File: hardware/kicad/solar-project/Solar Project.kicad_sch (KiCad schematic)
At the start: 129 parts, among them J1 Solar In, J3 Battery Bus, J4 JTAG, J5 Connector,_USB-TYPE-C-16P, M1 IPZ40N, M2 Q_NMOS, M3 Q_NMOS, M4 Q_NMOS, Q1 BSS138, Q2 BSS138, U1 STM32G431CBU6, U2 BSC112N06LD, U3 CP2102-GMR, U4 LM5163DDAR, U5 BSC155N06ND, U6 LM51772QRHARQ1, U7 AHT20

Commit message: Clean DRC and update handoff
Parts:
- removed J5: Connector,_USB-TYPE-C-16P, symbol 1My_parts - Connectors:Connector,_USB-TYPE-C-16P
- removed R1, R4: 5.1kΩ, PCM_JLCPCB:R_0805, symbol PCM_JLCPCB-Resistors:0805,5.1kΩ
- removed R19, R21: 10Ω, PCM_JLCPCB:R_0805, symbol PCM_JLCPCB-Resistors:0805,10Ω
- removed R24: 21.5k, digikey-footprints:0805, symbol Device:R
- removed TH1: Thermistor_NTC, symbol Device:Thermistor_NTC
- removed TP2: TestPoint_Small, symbol Connector:TestPoint_Small
- added 10mm1, 10mm2: ~, 1My_Parts_ Passive:10mm LOGO, symbol 1My_Passive:TNES_Logo_10mm
- added C47, C48, C51: 100nF, PCM_JLCPCB:C_0805, symbol PCM_JLCPCB-Capacitors:0805,100nF
- added C49, C50: 33pF, PCM_JLCPCB:C_0805, symbol PCM_JLCPCB-Capacitors:0805,33pF
- added J2: USB4105-GF-A, 1My_Parts_ Connectors:GCT_USB4105-GF-A, symbol 1My_Connectors:USB4105-GF-A
- added J5: Fan, Connector_JST:JST_PH_B3B-PH-K_1x03_P2.00mm_Vertical, symbol Connector:Conn_01x03_Socket
- added Q3: AO3400A, PCM_JLCPCB:Q_SOT-23, symbol PCM_JLCPCB-Transistors:NMOS,AO3400A
- added R1: 100kΩ, PCM_JLCPCB:R_0805, symbol PCM_JLCPCB-Resistors:0805,100kΩ
- added R19, R47, R48, R50, R53, R59: 10kΩ, PCM_JLCPCB:R_0805, symbol PCM_JLCPCB-Resistors:0805,10kΩ
- added R21: 102k, PCM_JLCPCB:R_0805, symbol Device:R
- added R24, R62: 5.1kΩ, PCM_JLCPCB:R_0805, symbol PCM_JLCPCB-Resistors:0805,5.1kΩ
- added R4: 10Ω, PCM_JLCPCB:R_0805, symbol PCM_JLCPCB-Resistors:0805,10Ω
- added R49, R63, R64: 0Ω, PCM_JLCPCB:R_0805, symbol PCM_JLCPCB-Resistors:0805,0Ω
- added R51: 2.7kΩ, PCM_JLCPCB:R_0805, symbol PCM_JLCPCB-Resistors:0805,2.7kΩ
- added R52: 1kΩ, PCM_JLCPCB:R_0805, symbol PCM_JLCPCB-Resistors:0805,1kΩ
- added R54, R55, R56, R57, R58: 10kΩ, PCM_JLCPCB:R_0805, symbol PCM_JLCPCB-Resistors_1:0805,10kΩ
- added R60: 1.5kΩ, PCM_JLCPCB:R_0805, symbol PCM_JLCPCB-Resistors:0805,1.5kΩ
- added R61: 20kΩ, PCM_JLCPCB:R_0805, symbol PCM_JLCPCB-Resistors:0805,20kΩ
- added S1: Tactile Button, 160gf, PCM_JLCPCB:SW_TS-1088-AR02016, symbol PCM_JLCPCB-Connectors_Buttons:Tactile Button, 160gf, 12V, 50mA, 4.0mm
- added SW1, SW2, SW3, SW4, SW5: Tactile Button, 160gf, PCM_JLCPCB:SW-SMD_4P-L5.1-W5.1-P3.70-LS6.5-TL-2, symbol PCM_JLCPCB-Connectors_Buttons:Tactile Button, 160gf, 12V, 50mA, 5.1mm
- added U10: INA213AIDCKR, PCM_JLCPCB:SOT-363_SC-70-6, symbol 1My_IC's:INA213AIDCKR
- added U9: LMV393, Package_SO:SOIC-8-1EP_3.9x4.9mm_P1.27mm_EP2.29x3mm_ThermalVias, symbol 1My_IC's:LMV393
- added X2: X49SM8MSD2SC, PCM_JLCPCB:CRYSTAL-SMD_L11.5-W4.8-LS12.7, symbol PCM_JLCPCB-Crystals:Crystal, 8MHz, 20pF, ±20ppm
- D3: footprint digikey-footprints:SOT23-6L -> Package_TO_SOT_SMD:SOT-23-6; symbol dk_TVS-Diodes:USBLC6-2SC6 -> Power_Protection:USBLC6-2SC6
- F2: footprint (none) -> Fuse:Fuseholder_Littelfuse_100_series_5x25mm
- J1, J3: footprint (none) -> TerminalBlock_Phoenix:TerminalBlock_Phoenix_MKDS-1,5-2-5.08_1x02_P5.08mm_Horizontal
- J4: footprint (none) -> Connector_PinHeader_2.54mm:PinHeader_1x04_P2.54mm_Vertical_SMD_Pin1Right
- L2: footprint (none) -> 1My_Parts_ Passive:HC3-1R0-R; LCSC (none) -> C2638566
- M1: symbol Device:Q_NMOS -> 1My_Basic components:IPZ40N
- M2, M3, M4: value Q_NMOS -> IPZ40N; footprint (none) -> Package_TO_SOT_SMD:TDSON-8-1; symbol Device:Q_NMOS -> 1My_Basic components:IPZ40N; LCSC (none) -> C6969335
- R16: footprint (none) -> 1My_Parts_ Passive:R_2512 Shunt 4 pad resistor; LCSC (none) -> C41382682
- R17: footprint (none) -> PCM_JLCPCB:R_0805; LCSC (none) -> C21437
- R18: footprint (none) -> PCM_JLCPCB:R_0805; LCSC (none) -> C2090706
- R20: value 0.010 -> 499kΩ; footprint 2818 -> PCM_JLCPCB:R_0805; LCSC C53115042 -> C17721
- R22: footprint (none) -> Resistor_SMD:R_Shunt_Vishay_WSK2512_6332Metric_T2.66mm; LCSC (none) -> C41382682
- R23: value 75k -> 75kΩ; footprint (none) -> PCM_JLCPCB:R_0805; symbol Device:R -> PCM_JLCPCB-Resistors:0805,75kΩ; Attrition Qty (none) -> 10; Category (none) -> Resistors,Chip Resistor - Surface Mount; Class (none) -> Preferred Component; LCSC (none) -> C17819; Manufacturer (none) -> UNI-ROYAL(Uniroyal Elec); Minimum Qty (none) -> 20; Operating Temperature Range (none) -> -55°C~+155°C; Overload Voltage (Max) (none) -> 150V; Part (none) -> 0805W8F7502T5E; Power(Watts) (none) -> 125mW; Price (none) -> 0.005USD; Process (none) -> SMT; Resistance (none) -> 75kΩ; Stock (none) -> 314874; Temperature Coefficient (none) -> ±100ppm/°C; Tolerance (none) -> ±1%; Type (none) -> Thick Film Resistors
- R25: footprint (none) -> PCM_JLCPCB:R_0805; LCSC (none) -> C2933470
- R28: footprint (none) -> PCM_JLCPCB:R_0603; LCSC (none) -> C863146
- R29: footprint (none) -> PCM_JLCPCB:R_0805; LCSC (none) -> C2077356
- R3: footprint digikey-footprints:0805 -> PCM_JLCPCB:R_0805
- R30: footprint (none) -> PCM_JLCPCB:R_0805; LCSC (none) -> C1854698
- R31: footprint (none) -> PCM_JLCPCB:R_0805; LCSC (none) -> C54532105
- R33: footprint (none) -> PCM_JLCPCB:R_0805; LCSC (none) -> C55098625
- TP1, TP3, TP4, TP5: footprint (none) -> Connector_PinHeader_2.54mm:PinHeader_1x01_P2.54mm_Vertical
- U1: footprint STM32G431CBU6:QFN50P700X700X60-49N -> Package_DFN_QFN:QFN-48-1EP_6x6mm_P0.4mm_EP4.4x4.4mm_ThermalVias
- U2, U5: footprint Package_SON:Infineon_PG-TDSON-8_6.15x5.15mm -> 1My_Parts_ ICs:Infineon_PG-TDSON-8
- U4: footprint PCM_JLCPCB:ESOP-8_L4.9-W3.9-P1.27-LS6.0-BL-EP -> Package_SO:Texas_R-PDSO-G8_EP2.95x4.9mm_Mask2.4x3.1mm_ThermalVias
- U7: footprint AHT20:PSON100P300X300X110-6N -> 1My_Parts_ ICs:Humidity sensor
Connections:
- net _CSA_2 is gone; now on net SW_1: R22.3, R26.1
- net BAT_BUS_POS: now also J3.2 (Pin_2)
- net CHG_OUT_POS: now also U5.6 (D1), J5.1 (Pin_1); no longer U5.7 (D2), U5.8 (D2)
- net CTS: now also U1.33 (PA11)
- net FAULT_OCP: now also U1.17 (PB0), R53.2, U9.7
- net FAULT_OVP: now also U1.18 (PB1), R19.2, U9.1
- net HO1: now also M1.4 (G); no longer M1.G
- net HO2: now also M4.4 (G); no longer M4.G
- net LO1: now also M2.4 (G); no longer M2.G
- net LO2: now also M3.4 (G); no longer M3.G
- net PV_IN_POS: now also C38.1, C39.1, C40.1, C41.1, C43.1, M1.5 (D), U2.6 (D1); no longer C38.2, C39.2, C40.2, C41.2, C43.2, M1.D, U2.7 (D2), U2.8 (D2)
- net PV_IN_POS_FUSED: no longer U2.6 (D1)
- net PWR_NEG: now also C30.2, C31.2, C34.2, C35.2, C38.2, C39.2, C4.2, C40.2, C41.2, C43.2, C6.2, J3.1 (Pin_1), M2.1 (S), M2.2 (S), M2.3 (S), M3.1 (S), M3.2 (S), M3.3 (S), U4.9 (TH_pd), C47.2, C48.2, C49.2, C50.2, C51.1, J2.A1_B12 (GND), J2.B1_A12 (GND__1), J2.SH1 (SHELL_GND), J2.SH2 (SHELL_GND__1), J2.SH3 (SHELL_GND__2), J2.SH4 (SHELL_GND__3), Q3.2 (S), R1.2, R24.1, R47.2, R48.2, R50.2, R52.2, R60.2, R62.1, S1.2 (B), SW1.3 (C), SW1.4 (D), SW2.3 (C), SW2.4 (D), SW3.3 (C), SW3.4 (D), SW4.3 (C), SW4.4 (D), SW5.3 (C), SW5.4 (D), U10.1 (REF), U10.2 (GND), U9.4 (V-), U9.9 (EP); no longer C30.1, C31.1, C34.1, C35.1, C38.1, C39.1, C4.1, C40.1, C41.1, C43.1, C6.1, J3.2 (Pin_2), M2.S, M3.S
- net RTS: now also U1.34 (PA12)
- net SW_1: now also M1.1 (S), M1.2 (S), M1.3 (S), M2.5 (D); no longer M1.S, M2.D
- net SW_2: now also M3.5 (D), M4.1 (S), M4.2 (S), M4.3 (S); no longer M3.D, M4.S
- net U6_FLT: now also U1.2 (PC13)
- net VBUS: now also J2.A4_B9 (VBUS), J2.B4_A9 (VBUS__1)
- net V_out: now also C30.1, C31.1, C34.1, C35.1, C4.1, C6.1, M4.5 (D), R16.3, R64.2, U10.4 (IN+); no longer C30.2, C31.2, C34.2, C35.2, C4.2, C6.2, M4.D
- net _CSB_2: now also L2.1, R22.1
- net _Undervoltage Feedback: now also R61.1
- net V_out_sense: now reaches R16.1, R38.1, TP1.1, U5.5 (D1)
- net V_out_sense: now also R16.2, R63.2, U10.5 (IN-); no longer U5.6 (D1)
- net at D3.1 (I/O1): now also U3.4 (D+)
- net at D3.3 (I/O2): now also J2.A6 (DP1), J2.B6 (DP2)
- net at D3.4 (I/O2): now also J2.A7 (DN1), J2.B7 (DN2); no longer U3.4 (D+)
- net BTN_RT_N: now reaches U1.3 (PC14-OSC32_IN)
- net BTN_RT_N: now also SW3.1 (A)
- net BTN_UP_N: now reaches U1.38 (PA15)
- net BTN_UP_N: now also SW1.1 (A)
- net Fan Control: now reaches U1.40 (PC11)
- net Fan Control: now also R4.1
- net BTN_DN_N: now reaches U1.41 (PB3)
- net BTN_DN_N: now also SW2.1 (A)
- net BTN_LT_N: now reaches U1.42 (PB4)
- net BTN_LT_N: now also SW4.1 (A)
- net BTN_ENT_N: now reaches U1.47 (PB9)
- net BTN_ENT_N: now also SW5.1 (A)
- net at U1.5 (PF0-OSC_IN): now also C50.1, X2.1
- net at U1.6 (PF1-OSC_OUT): now also C49.1, X2.2
- net at U1.7 (PG10-~{RST}): now also C47.1, R59.2, S1.1 (A)
- net OVP_SENSE: now reaches R20.2
- net OVP_SENSE: now also R47.1, U9.3 (+); no longer J3.1 (Pin_1)
- net CTRL_SUPPLY_IN: no longer names the net of C15.1, D4.1, D6.1, D7.1, R13.1, U4.2 (VIN)
- net ISNSN: no longer names the net of U6.19 (ISNSN)
- net ISNSN: now also R63.1; no longer R16.2
- net ISNSP: no longer names the net of U6.20 (ISNSP)
- net ISNSP: now also R64.1; no longer R16.3
- net SENSE_TEMP_PWR: no longer names the net of U1.14 (PA6)
- net VDD renamed CTRL_3V3
- net CTRL_3V3: now also C48.1, C51.2, R19.1, R21.1, R51.1, R53.1, R54.1, R55.1, R56.1, R57.1, R58.1, R59.1, U10.3 (V+), U9.8 (V+)
- new net: R56.2, SW3.2 (B)
- new net: Q3.1 (G), R1.1, R4.2
- new net: R54.2, SW1.2 (B)
- new net: R57.2, SW4.2 (B)
- new net: J2.A5 (CC1), R24.2
- new net: J2.A8 (SBU1), J2.B8 (SBU2)
- new net: J2.B5 (CC2), R62.2
- new net: R55.2, SW2.2 (B)
- new net: R58.2, SW5.2 (B)
- new net: R60.1, R61.2
- new net: J5.3 (Pin_3), Q3.3 (D)
- new net OCP_MEAS: R49.1, U10.6 (OUT)
- new net OCP_REF: R51.2, R52.1, U9.6 (-)
- new net OCP_SENSE: R49.2, R50.1, U9.5 (+)
- new net OVP_REF: R21.2, R48.1, U9.2 (-)
- no-connect marks 56 -> 44
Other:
- note added: "3.3V control"
- note added: "Fan Control"
- note added: "Nav Buttons"
- note added: "Output Protection"
- note removed: "UART 1 and power"
- company: (none) -> True North Enterprise Solutions LLC
- title: (none) -> Solar Charge Controller
- moved on the sheet: C1, C10, C11, C12, C14, C15, C16, C17, C18, C19, C2, C20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

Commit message: Update Rev 0 hardware status and docs
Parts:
- F1: value 10 amp -> Fuse_TD_10A_5x25_63VDC_MIN; Part - USA (none) -> TBD
- F2: LCSC (none) -> C142864
- J1, J3: LCSC (none) -> C8439
- J2: LCSC (none) -> C3020560
- J4: LCSC (none) -> C41417361
- J5: footprint Connector_JST:JST_PH_B3B-PH-K_1x03_P2.00mm_Vertical -> Connector_PinHeader_2.54mm:PinHeader_1x03_P2.54mm_Vertical; LCSC (none) -> C2937625
- TP1, TP3, TP4, TP5: now not fitted; now left out of the parts list
- U1: value STM32G431CBU6 -> STM32F411CEU6; footprint Package_DFN_QFN:QFN-48-1EP_6x6mm_P0.4mm_EP4.4x4.4mm_ThermalVias -> Package_DFN_QFN:QFN-48-1EP_7x7mm_P0.5mm_EP5.6x5.6mm; Check_prices https://www.snapeda.com/parts/STM32G431CBU6/STMicroelectron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 -> https://www.snapeda.com/parts/STM32F411CEU6/STMicroelectron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; LCSC (none) -> C529356; MP STM32G431CBU6 -> STM32F411CEU6; Purchase-URL https://www.snapeda.com/api/url_track_click_mouser/?unipart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 -> https://www.snapeda.com/api/url_track_click_mouser/?manufac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; SnapEDA_Link https://www.snapeda.com/parts/STM32G431CBU6/STMicroelectron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 -> https://www.snapeda.com/parts/STM32F411CEU6/STMicroelectron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
- U7: LCSC (none) -> C2757850
- U8: LCSC (none) -> C5248080
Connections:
- net PWR_NEG: now also U1.24 (PB11)
- no-connect marks 44 -> 43
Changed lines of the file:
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@@
 	)
 	(no_connect
-		(at 289.56 190.5)
-	)
-	(no_connect
 		(at 289.56 210.82)
 	)
@@
 		)
 	)
+	(global_label "PWR_NEG"
+		(shape input)
+		(at 289.56 190.5 0)
+		(fields_autoplaced yes)
+		(effects
+			(font
+				(size 0.635 0.635)
+			)
+			(justify left)
+		)
+		(property "Intersheetrefs" "${INTERSHEET_REFS}"
+			(at 295.4069 190.5 0)
+			(effects
+				(font
+					(size 1.27 1.27)
+				)
+				(justify left)
+				(hide yes)
+			)
+		)
+	)
 	(global_label "TXD"
 		(shape tri_state)
@@
 		(on_board yes)
 		(dnp no)
-		(fields_autoplaced yes)
 		(property "Reference" "F1"
 			(at 48.26 78.7399 0)
@@
 			)
 		)
-		(property "Value" "10 amp"
-			(at 48.26 81.2799 0)
+		(property "Value" "Fuse_TD_10A_5x25_63VDC_MIN"
+			(at 35.052 79.502 0)
 			(effects
 				(font
-					(size 1.27 1.27)
+					(size 0.8 0.8)
 				)
 				(justify left)
@@
 			)
 		)
-		(property "Datasheet" "~"
+		(property "Datasheet" "https://www.lcsc.com/datasheet/C142864.pdf?spm=wm.sxq.inf.ggs&lcsc_vid=EVEIA1dfFlIMBAdXEgVXUVVVTwRWBgBfE1lbBABSQFMxVlNeQ1hXX1RUTlVdVTsOAxUeFF5JWBYZEEoKFBINSQcJGk4NBhADEA4cHktXRVJADxALGw%3D%3D"
 			(at 45.72 80.01 0)
 			(effects
@@
 			)
 		)
-		(property "Description" "Fuse"
+		(property "Description" "TBD: 5x25mm time-delay fuse, 10A class, 63VDC minimum"
 			(at 45.72 80.01 0)
 			(effects
@@
 			)
 		)
-		(property "Part - USA" ""
+		(property "Part - USA" "TBD"
 			(at 45.72 80.01 0)
 			(effects
@@
 			)
 		)
-		(property "Datasheet" "~"
+		(property "Datasheet" "https://www.lcsc.com/datasheet/C142864.pdf?spm=wm.sxq.inf.ggs&lcsc_vid=EVEIA1dfFlIMBAdXEgVXUVVVTwRWBgBfE1lbBABSQFMxVlNeQ1hXX1RUTlVdVTsOAxUeFF5JWBYZEEoKFBINSQcJGk4NBhADEA4cHktXRVJADxALGw%3D%3D"
 			(at 414.02 60.96 0)
 			(effects
@@
 			)
 		)
+		(property "LCSC" "C142864"
+			(at 414.02 60.96 0)
+			(effects
+				(font
+					(size 1.27 1.27)
+				)
+				(hide yes)
+			)
+		)
 		(pin "1"
 		)
@@
 		(unit 1)
 		(exclude_from_sim no)
-		(in_bom yes)
+		(in_bom no)
 		(on_board yes)
-		(dnp no)
+		(dnp yes)
 		(fields_autoplaced yes)
 		(property "Reference" "TP4"
@@
 			)
 		)
-		(property "Datasheet" ""
+		(property "Datasheet" "https://www.lcsc.com/datasheet/C3020560.pdf?spm=wm.sxq.inf.ggs___wm.ssy.em.0.tz&lcsc_vid=EVEIA1dfFlIMBAdXEgVXUVVVTwRWBgBfE1lbBABSQFMxVlNeQ1hXUVFWQlBdVDsOAxUeFF5JWBYZEEoKFBINSQcJGk4dAgUUFAk%3D"
 			(at 63.5 334.01 0)
 			(effects
@@
 			)
 		)
+		(property "LCSC" "C3020560"
+			(at 63.5 334.01 0)
+			(effects
+				(font
+					(size 1.27 1.27)
+				)
+				(hide yes)
+			)
+		)
 		(pin "A1_B12"
 		)
@@
 			)
 		)
-		(property "Datasheet" ""
+		(property "Datasheet" "https://www.lcsc.com/datasheet/C5248080.pdf?spm=wm.sxq.inf.ggs___wm.fly.bg.0.xh&lcsc_vid=EVEIA1dfFlIMBAdXEgVXUVVVTwRWBgBfE1lbBABSQFMxVlNeQlFeUV1eQllaVDsOAxUeFF5JWBYZEEoKFBINSQcJGk4eFQsCAgIaSgADAwAHC0slRVZbUFxTR08GEwkK"
 			(at 382.27 346.71 0)
 			(effects
@@
 			)
 		)
+		(property "LCSC" "C5248080"
+			(at 382.27 334.01 0)
+			(effects
+				(font
+					(size 1.27 1.27)
+				)
+				(hide yes)
+			)
+		)
 		(pin "7"
 		)
@@
 			)
 		)
-		(property "Value" "STM32G431CBU6"
+		(property "Value" "STM32F411CEU6"
 			(at 266.7 160.02 0)
 			(effects
@@
 			)
 		)
-		(property "Footprint" "Package_DFN_QFN:QFN-48-1EP_6x6mm_P0.4mm_EP4.4x4.4mm_ThermalVias"
+		(property "Footprint" "Package_DFN_QFN:QFN-48-1EP_7x7mm_P0.5mm_EP5.6x5.6mm"
 			(at 266.7 203.2 0)
 			(effects
@@
 			)
 		)
-		(property "Datasheet" ""
+		(property "Datasheet" "https://www.lcsc.com/datasheet/C529356.pdf?spm=wm.sxq.inf.ggs___wm.fly.bg.0.xh&lcsc_vid=EVEIA1dfFlIMBAdXEgVXUVVVTwRWBgBfE1lbBABSQFMxVlNeQ1hXXlxeRlNZXjsOAxUeFF5JWBYZEEoKFBINSQcJGk4eFQsCAgIaSgADAwAHC0slRVhdUFJUQk8GEwkK"
 			(at 266.7 203.2 0)
 			(effects
@@
 			)
 		)
-		(property "Description" ""
+		(property "Description" "Arm Cortex-M4 32-bit MCU+FPU, 170 MHz / 213 DMIPS, up to 128 KB Flash, 32 KB SRAM, rich analog, math accelerator"
 			(at 266.7 203.2 0)
 			(effects
@@
 			)
 		)
-		(property "Check_prices" "https://www.snapeda.com/parts/STM32G431CBU6/STMicroelectronics/view-part/?ref=eda"
+		(property "Check_prices" "https://www.snapeda.com/parts/STM32F411CEU6/STMicroelectronics/view-part/?ref=eda"
 			(at 266.7 203.2 0)
 			(effects
@@
 			)
 		)
-		(property "SnapEDA_Link" "https://www.snapeda.com/parts/STM32G431CBU6/STMicroelectronics/view-part/?ref=snap"
+		(property "SnapEDA_Link" "https://www.snapeda.com/parts/STM32F411CEU6/STMicroelectronics/view-part/?ref=snap"
 			(at 266.7 203.2 0)
 			(effects
@@
 			)
 		)
-		(property "MP" "STM32G431CBU6"
+		(property "MP" "STM32F411CEU6"
 			(at 266.7 203.2 0)
 			(effects
@@
 			)
 		)
-		(property "Purchase-URL" "https://www.snapeda.com/api/url_track_click_mouser/?unipart_id=3657449&manufacturer=STMicroelectronics&part_name=STM32G431CBU6&search_term=stm32g431"
+		(property "Purchase-URL" "https://www.snapeda.com/api/url_track_click_mouser/?manufacturer=STMicroelectronics&part_name=STM32F411CEU6&search_term=stm32f411"
 			(at 266.7 203.2 0)
 			(effects
@@
 			)
 		)
+		(property "LCSC" "C529356"
+			(at 266.7 203.2 0)
+			(effects
+				(font
+					(size 1.27 1.27)
+				)
+				(hide yes)
+			)
+		)
 		(pin "26"
 		)
@@
 			)
 		)
-		(property "Datasheet" "~"
+		(property "Datasheet" "https://www.lcsc.com/datasheet/C8439.pdf?spm=wm.sxq.inf.ggs___wm.fly.bg.6.xh&lcsc_vid=EVEIA1dfFlIMBAdXEgVXUVVVTwRWBgBfE1lbBABSQFMxVlNeQ1hXUFVURlFZUjsOAxUeFF5JWBYZEEoKFBINSQcJGk4NBhADEA4cHktXQFVADxALGw%3D%3D"
 			(at 40.64 90.17 0)
 			(effects
@@
 			)
 		)
+		(property "LCSC" "C8439"
+			(at 40.64 90.17 0)
+			(effects
+				(font
+					(size 1.27 1.27)
+				)
+				(hide yes)
+			)
+		)
 		(pin "2"
 		)
@@
 		(unit 1)
 		(exclude_from_sim no)
-		(in_bom yes)
+		(in_bom no)
 		(on_board yes)
-		(dnp no)
+		(dnp yes)
 		(fields_autoplaced yes)
 		(property "Reference" "TP1"
@@
 			)
 		)
-		(property "Datasheet" "~"
+		(property "Datasheet" "https://www.lcsc.com/datasheet/C8439.pdf?spm=wm.sxq.inf.ggs___wm.fly.bg.6.xh&lcsc_vid=EVEIA1dfFlIMBAdXEgVXUVVVTwRWBgBfE1lbBABSQFMxVlNeQ1hXUFVURlFZUjsOAxUeFF5JWBYZEEoKFBINSQcJGk4NBhADEA4cHktXQFVADxALGw%3D%3D"
 			(at 419.1 91.44 0)
 			(effects
@@
 			)
 		)
+		(property "LCSC" "C8439"
+			(at 419.1 91.44 0)
+			(effects
+				(font
+					(size 1.27 1.27)
+				)
+				(hide yes)
+			)
+		)
 		(pin "2"
 		)
@@
 		(unit 1)
 		(exclude_from_sim no)
-		(in_bom yes)
+		(in_bom no)
 		(on_board yes)
-		(dnp no)
+		(dnp yes)
 		(fields_autoplaced yes)
 		(property "Reference" "TP5"
@@
 		(unit 1)
 		(exclude_from_sim no)
-		(in_bom yes)
+		(in_bom no)
 		(on_board yes)
-		(dnp no)
+		(dnp yes)
 		(fields_autoplaced yes)
 		(property "Reference" "TP3"
@@
 			)
 		)
-		(property "Footprint" "Connector_JST:JST_PH_B3B-PH-K_1x03_P2.00mm_Vertical"
+		(property "Footprint" "Connector_PinHeader_2.54mm:PinHeader_1x03_P2.54mm_Vertical"
 			(at 453.39 321.31 0)
 			(effects
@@
 			)
 		)
-		(property "Datasheet" "~"
+		(property "Datasheet" "https://www.lcsc.com/datasheet/C2937625.pdf?spm=wm.sxq.inf.ggs___wm.fly.bg.0.xh&lcsc_vid=EVEIA1dfFlIMBAdXEgVXUVVVTwRWBgBfE1lbBABSQFMxVlNeQ1hXXldVQ1VdVjsOAxUeFF5JWBYZEEoKFBINSQcJGk4NBhADEA4cHktRTlNADxALGw%3D%3D"
 			(at 453.39 321.31 0)
 			(effects
@@
 			)
 		)
+		(property "LCSC" "C2937625"
+			(at 453.39 321.31 0)
+			(effects
+				(font
+					(size 1.27 1.27)
+				)
+				(hide yes)
+			)
+		)
 		(pin "2"
 		)
@@
 			)
 		)
-		(property "Datasheet" ""
+		(property "Datasheet" "https://www.lcsc.com/datasheet/C2757850.pdf?spm=wm.sxq.inf.ggs___wm.fly.bg.0.cbh&lcsc_vid=EVEIA1dfFlIMBAdXEgVXUVVVTwRWBgBfE1lbBABSQFMxVlNeQlFeUVxTRFZZVzsOAxUeFF5JWBYZEEoKFBINSQcJGk4dAgUUFAk%3D"
 			(at 255.27 369.57 0)
 			(effects
@@
 			)
 		)
+		(property "LCSC" "C2757850"
+			(at 255.27 369.57 0)
+			(effects
+				(font
+					(size 1.27 1.27)
+				)
+				(hide yes)
+			)
+		)
 		(pin "3"
 		)
@@
 			)
 		)
-		(property "Datasheet" "~"
+		(property "Datasheet" "~https://www.lcsc.com/datasheet/C41417361.pdf?spm=wm.sxq.inf.ggs___wm.fly.bg.1.xh&lcsc_vid=EVEIA1dfFlIMBAdXEgVXUVVVTwRWBgBfE1lbBABSQFMxVlNeQ1hXX1BTQlBXVDsOAxUeFF5JWBYZEEoKFBINSQcJGk4eFQsCAgIaSgADAwAHC0slRlVcX1JSWQkaCgg%3D"
 			(at 266.7 254 0)
 			(effects
@@
 			(at 266.7 254 0)
 			(effects
+				(font
+					(size 1.27 1.27)
+				)
+				(hide yes)
+			)
+		)
+		(property "LCSC" "C41417361"
+			(at 266.7 254 0)
+			(effects

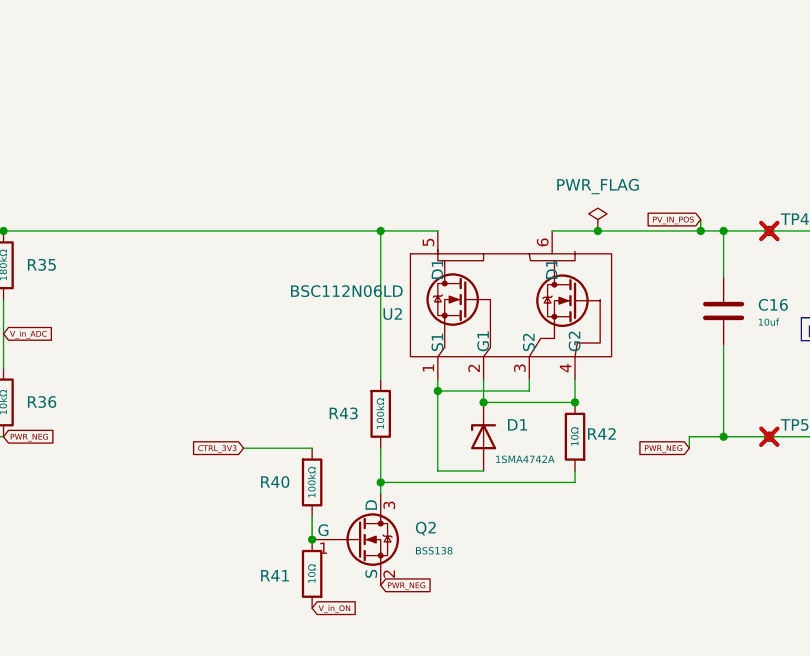
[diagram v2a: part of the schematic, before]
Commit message: Add SPICE harness baseline and refresh project handoffs
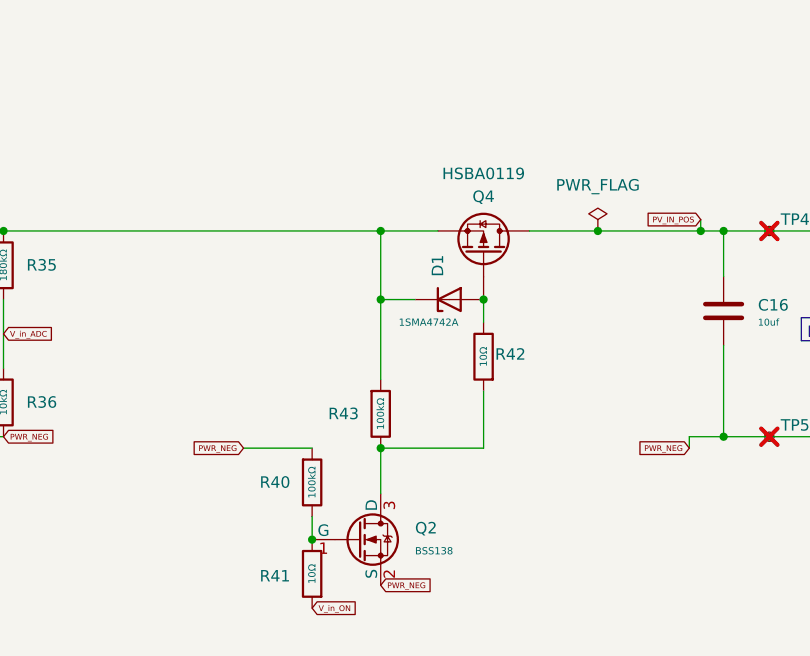
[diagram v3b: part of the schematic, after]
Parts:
- removed U2: BSC112N06LD, 1My_Parts_ ICs:Infineon_PG-TDSON-8, symbol 1My_Basic components:BSC112N06LD
- added Q4: HSBA0119, PRPAK-8(5x6), symbol Device:Q_PMOS
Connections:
- net CTRL_3V3: no longer R40.1
- net PV_IN_POS: now also Q4.D
- net PV_IN_POS_FUSED: now also D1.1, Q4.S
- net PWR_NEG: now also R40.1
- net at R42.2: now also D1.2, Q4.G; no longer D1.1
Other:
- moved on the sheet: D1, R42
